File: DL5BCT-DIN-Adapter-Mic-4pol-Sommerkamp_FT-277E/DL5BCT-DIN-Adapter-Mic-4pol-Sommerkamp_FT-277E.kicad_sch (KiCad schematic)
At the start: 1 part

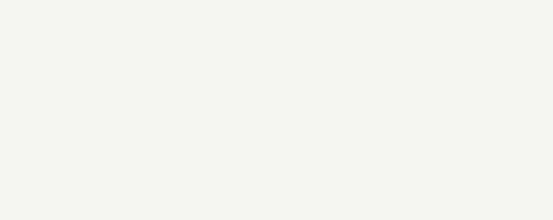
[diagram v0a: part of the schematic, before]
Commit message: Added new local schematics library for new symbols. 	modified:   DL5BCT-DIN-Adapter-Mic-4pol-Sommerkamp_FT-277E/DL5BCT-DIN-Adapter-Mic-4pol-Sommerkamp_FT-277E.kicad_sch 	new file:   DL5BCT-DIN-Adapter-Mic-4pol-Sommerkamp_FT-277E/sym-lib-table 	new file:   DL5BCT-DIN-Standard.bak 	new file:   DL5BCT-DIN-Standard.kicad_sym
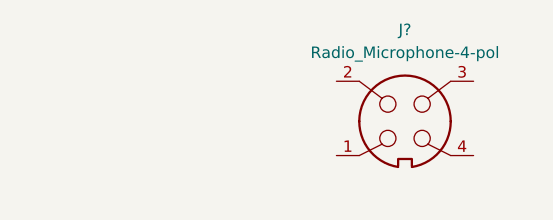
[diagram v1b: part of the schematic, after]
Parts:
- added J?: Radio_Microphone-4-pol, symbol DL5BCT-DIN-Standard:Radio_Microphone-4-pol
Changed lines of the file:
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@@
     (pin "5")
+  )
+  (symbol (lib_id "DL5BCT-DIN-Standard:Radio_Microphone-4-pol") (at 182.88 90.17 0) (unit 1)
+    (in_bom yes) (on_board yes) (fields_autoplaced)
+    (property "Reference" "J?" (id 0) (at 190.5 76.2 0))
+    (property "Value" "Radio_Microphone-4-pol" (id 1) (at 190.5 78.74 0))
+    (property "Footprint" "" (id 2) (at 190.5 86.36 0)
+      (effects (font (size 1.27 1.27)) hide)
+    )
+    (property "Datasheet" "(TBD)" (id 3) (at 190.5 95.25 0)
+      (effects (font (size 1.27 1.27)) hide)
+    )
+    (pin "1")
+    (pin "2")
+    (pin "3")
+    (pin "4")
   )
   (sheet_instances
@@
       (reference "J?") (unit 1) (value "DIN-5_180degree") (footprint "")
     )
+    (path "/8333ab48-756e-44fd-9bca-2278a8572e12"
+      (reference "J?") (unit 1) (value "Radio_Microphone-4-pol") (footprint "")
+    )
   )

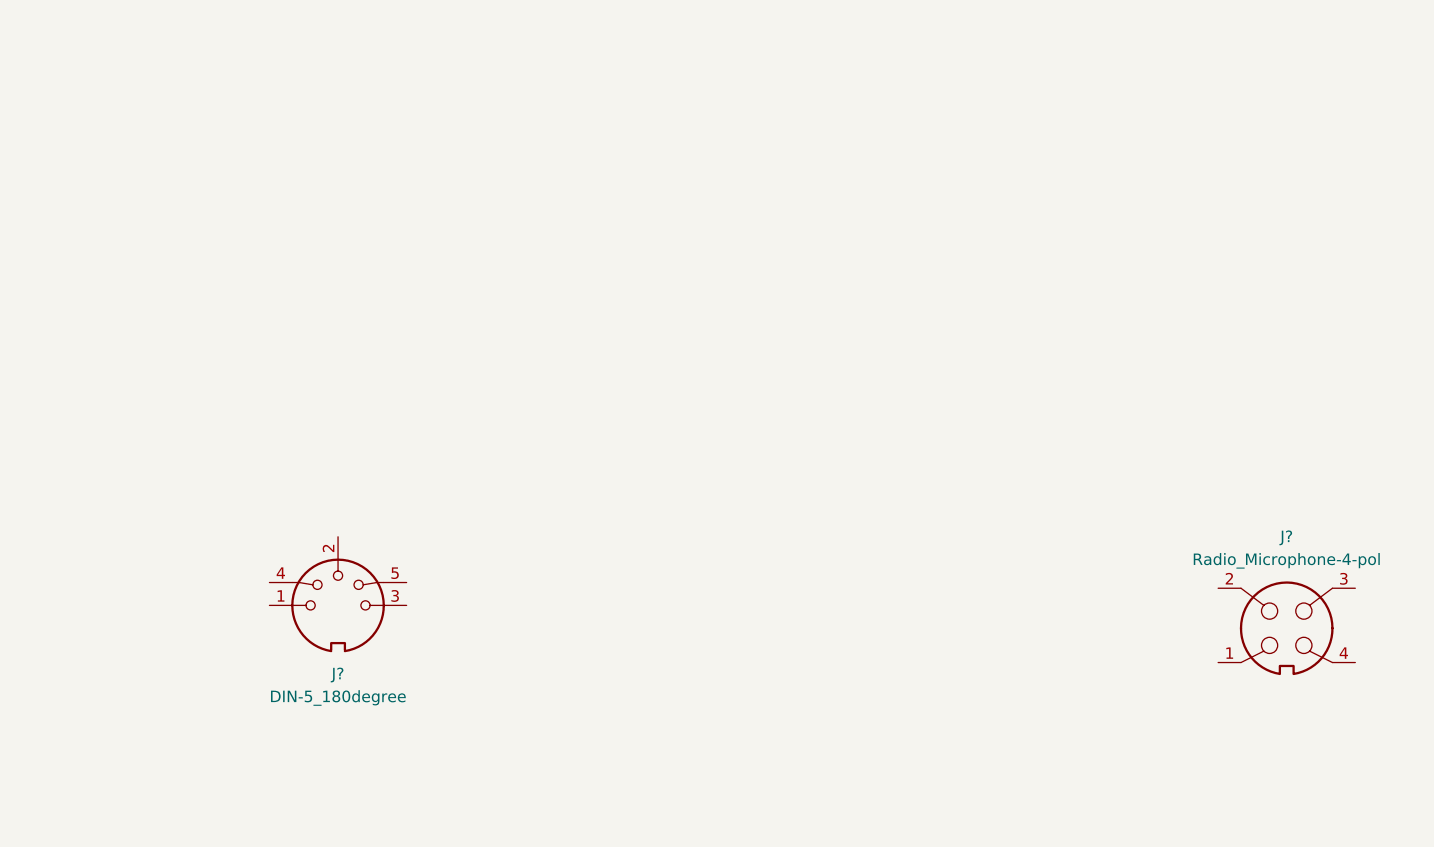
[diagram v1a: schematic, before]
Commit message: Complete adapter drawing. 	new file:   DL5BCT-DIN-Adapter-Mic-4pol-Sommerkamp_FT-277E/DL5BCT-DIN-Adapter-Mic-4pol-Sommerkamp_FT-277E.csv 	modified:   DL5BCT-DIN-Adapter-Mic-4pol-Sommerkamp_FT-277E/DL5BCT-DIN-Adapter-Mic-4pol-Sommerkamp_FT-277E.kicad_sch 	new file:   DL5BCT-DIN-Adapter-Mic-4pol-Sommerkamp_FT-277E/DL5BCT-DIN-Adapter-Mic-4pol-Sommerkamp_FT-277E.xml 	modified:   DL5BCT-DIN-Standard.bak 	modified:   DL5BCT-DIN-Standard.kicad_sym
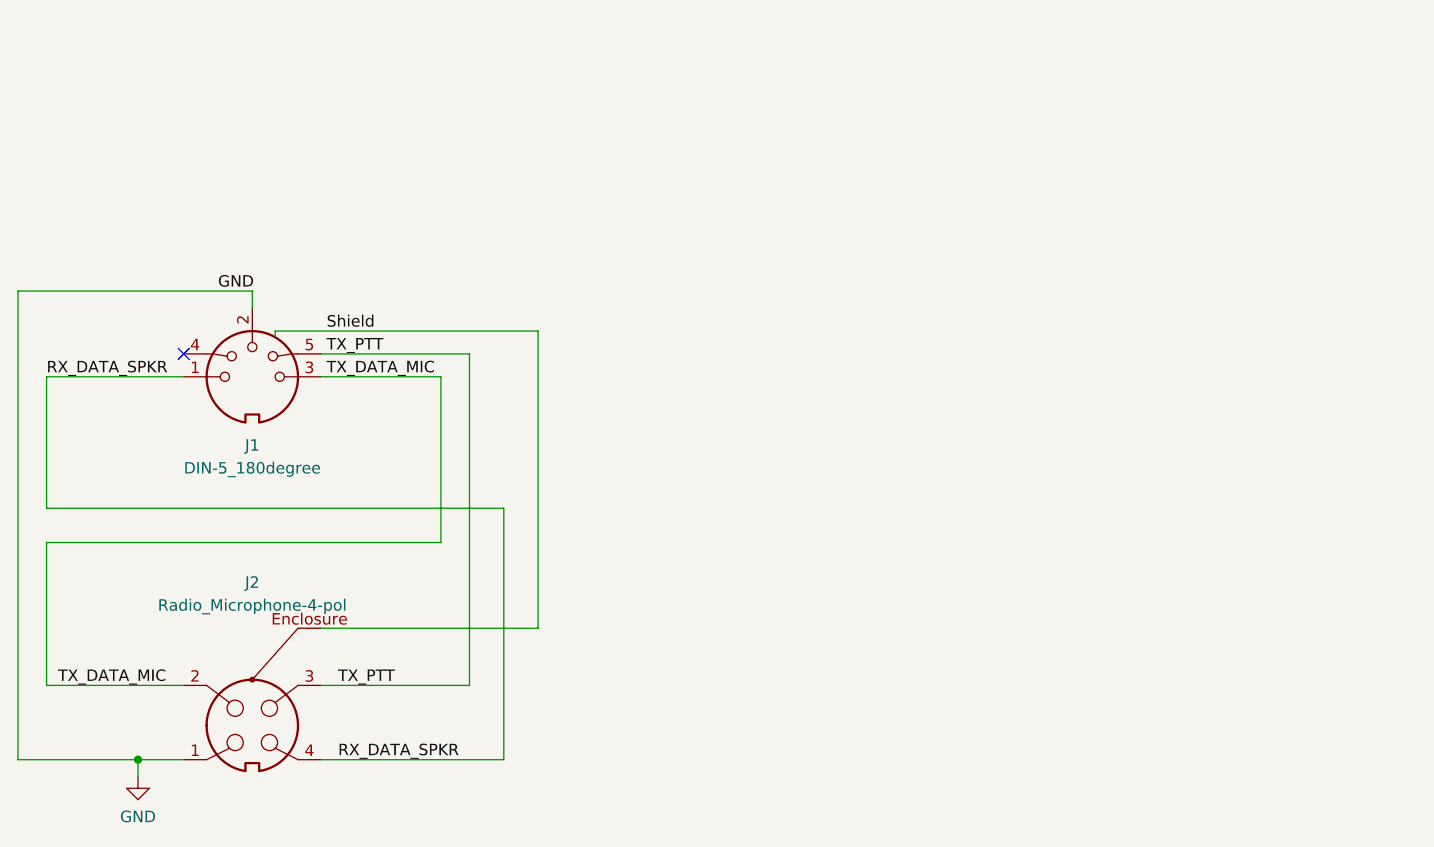
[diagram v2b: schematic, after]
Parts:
- removed J?: Radio_Microphone-4-pol, symbol DL5BCT-DIN-Standard:Radio_Microphone-4-pol
- added J2: Radio_Microphone-4-pol, symbol DL5BCT-DIN-Standard:Radio_Microphone-4-pol
- gave numbers to parts that had none: 1
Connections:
- net RX_DATA_SPKR: now reaches J1.1
- net RX_DATA_SPKR: now also J2.4
- net GND: now reaches J1.2
- net GND: now also J2.1
- net TX_DATA_MIC: now reaches J1.3
- net TX_DATA_MIC: now also J2.2
- net TX_PTT: now reaches J1.5
- net TX_PTT: now also J2.3
- new net Shield: J2.Enclosure
- no-connect marks 0 -> 1
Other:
- company: (none) -> Peter Cornelius DL5BCT / peter cornelius consulting
- title: (none) -> Adapter DL5BCT-DIN-Standard <--> TRX MIC 4-pol
- moved on the sheet: J1
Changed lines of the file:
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@@
 (kicad_sch (version 20211123) (generator eeschema)
-  (paper "A4")
-  (symbol (lib_id "Connector:DIN-5_180degree") (at 85.09 83.82 0) (unit 1)
+  (paper "A5" portrait)
+  (title_block
+    (title "Adapter DL5BCT-DIN-Standard <--> TRX MIC 4-pol")
+    (date "2023-01-07")
+    (rev "1.0")
+    (company "Peter Cornelius DL5BCT / peter cornelius consulting")
+    (comment 1 "Adapter from/to DL5BCT DIN Standard to 4-pol TRX mike connector")
+    (comment 2 "Sommerkamp FT-277 E")
+  )
+  (junction (at 62.865 100.965) (diameter 0) (color 0 0 0 0)
+  )
+  (no_connect (at 67.945 55.88))
+  (wire (pts (xy 52.705 73.025) (xy 52.705 58.42))
+    (stroke (width 0) (type default) (color 0 0 0 0))
+  )
+  (wire (pts (xy 96.52 76.835) (xy 96.52 58.42))
+    (stroke (width 0) (type default) (color 0 0 0 0))
+  )
+  (wire (pts (xy 62.865 100.965) (xy 67.945 100.965))
+    (stroke (width 0) (type default) (color 0 0 0 0))
+  )
+  (wire (pts (xy 78.105 53.34) (xy 78.105 53.975))
+    (stroke (width 0) (type default) (color 0 0 0 0))
+  )
+  (wire (pts (xy 52.705 92.71) (xy 52.705 76.835))
+    (stroke (width 0) (type default) (color 0 0 0 0))
+  )
+  (wire (pts (xy 52.705 76.835) (xy 96.52 76.835))
+    (stroke (width 0) (type default) (color 0 0 0 0))
+  )
+  (wire (pts (xy 75.565 48.895) (xy 75.565 50.8))
+    (stroke (width 0) (type default) (color 0 0 0 0))
+  )
+  (wire (pts (xy 83.185 86.36) (xy 107.315 86.36))
+    (stroke (width 0) (type default) (color 0 0 0 0))
+  )
+  (wire (pts (xy 103.505 73.025) (xy 52.705 73.025))
+    (stroke (width 0) (type default) (color 0 0 0 0))
+  )
+  (wire (pts (xy 107.315 86.36) (xy 107.315 53.34))
+    (stroke (width 0) (type default) (color 0 0 0 0))
+  )
+  (wire (pts (xy 99.695 55.88) (xy 83.185 55.88))
+    (stroke (width 0) (type default) (color 0 0 0 0))
+  )
+  (wire (pts (xy 49.53 100.965) (xy 62.865 100.965))
+    (stroke (width 0) (type default) (color 0 0 0 0))
+  )
+  (wire (pts (xy 83.185 92.71) (xy 99.695 92.71))
+    (stroke (width 0) (type default) (color 0 0 0 0))
+  )
+  (wire (pts (xy 83.185 100.965) (xy 103.505 100.965))
+    (stroke (width 0) (type default) (color 0 0 0 0))
+  )
+  (wire (pts (xy 52.705 92.71) (xy 67.945 92.71))
+    (stroke (width 0) (type default) (color 0 0 0 0))
+  )
+  (wire (pts (xy 49.53 48.895) (xy 49.53 100.965))
+    (stroke (width 0) (type default) (color 0 0 0 0))
+  )
+  (wire (pts (xy 49.53 48.895) (xy 75.565 48.895))
+    (stroke (width 0) (type default) (color 0 0 0 0))
+  )
+  (wire (pts (xy 107.315 53.34) (xy 78.105 53.34))
+    (stroke (width 0) (type default) (color 0 0 0 0))
+  )
+  (wire (pts (xy 96.52 58.42) (xy 83.185 58.42))
+    (stroke (width 0) (type default) (color 0 0 0 0))
+  )
+  (wire (pts (xy 62.865 100.965) (xy 62.865 102.87))
+    (stroke (width 0) (type default) (color 0 0 0 0))
+  )
+  (wire (pts (xy 52.705 58.42) (xy 67.945 58.42))
+    (stroke (width 0) (type default) (color 0 0 0 0))
+  )
+  (wire (pts (xy 103.505 100.965) (xy 103.505 73.025))
+    (stroke (width 0) (type default) (color 0 0 0 0))
+  )
+  (wire (pts (xy 99.695 92.71) (xy 99.695 55.88))
+    (stroke (width 0) (type default) (color 0 0 0 0))
+  )
+  (label "Shield" (at 83.82 53.34 0)
+    (effects (font (size 1.27 1.27)) (justify left bottom))
+  )
+  (label "TX_PTT" (at 85.09 92.71 0)
+    (effects (font (size 1.27 1.27)) (justify left bottom))
+  )
+  (label "TX_DATA_MIC" (at 53.975 92.71 0)
+    (effects (font (size 1.27 1.27)) (justify left bottom))
+  )
+  (label "TX_PTT" (at 83.82 55.88 0)
+    (effects (font (size 1.27 1.27)) (justify left bottom))
+  )
+  (label "TX_DATA_MIC" (at 83.82 58.42 0)
+    (effects (font (size 1.27 1.27)) (justify left bottom))
+  )
+  (label "RX_DATA_SPKR" (at 52.705 58.42 0)
+    (effects (font (size 1.27 1.27)) (justify left bottom))
+  )
+  (label "RX_DATA_SPKR" (at 85.09 100.965 0)
+    (effects (font (size 1.27 1.27)) (justify left bottom))
+  )
+  (label "GND" (at 71.755 48.895 0)
+    (effects (font (size 1.27 1.27)) (justify left bottom))
+  )
+  (symbol (lib_id "Connector:DIN-5_180degree") (at 75.565 58.42 0) (unit 1)
     (in_bom yes) (on_board yes) (fields_autoplaced)
-    (property "Reference" "J?" (id 0) (at 85.0901 91.44 0))
-    (property "Value" "DIN-5_180degree" (id 1) (at 85.0901 93.98 0))
-    (property "Footprint" "" (id 2) (at 85.09 83.82 0)
+    (property "Reference" "J1" (id 0) (at 75.5651 66.04 0))
+    (property "Value" "DIN-5_180degree" (id 1) (at 75.5651 68.58 0))
+    (property "Footprint" "" (id 2) (at 75.565 58.42 0)
       (effects (font (size 1.27 1.27)) hide)
     )
-    (property "Datasheet" "http://www.mouser.com/ds/2/18/40_c091_abd_e-75918.pdf" (id 3) (at 85.09 83.82 0)
+    (property "Datasheet" "http://www.mouser.com/ds/2/18/40_c091_abd_e-75918.pdf" (id 3) (at 75.565 58.42 0)
       (effects (font (size 1.27 1.27)) hide)
     )
@@
     (pin "5")
   )
-  (symbol (lib_id "DL5BCT-DIN-Standard:Radio_Microphone-4-pol") (at 182.88 90.17 0) (unit 1)
+  (symbol (lib_id "DL5BCT-DIN-Standard:Radio_Microphone-4-pol") (at 67.945 100.965 0) (unit 1)
     (in_bom yes) (on_board yes) (fields_autoplaced)
-    (property "Reference" "J?" (id 0) (at 190.5 76.2 0))
-    (property "Value" "Radio_Microphone-4-pol" (id 1) (at 190.5 78.74 0))
-    (property "Footprint" "" (id 2) (at 190.5 86.36 0)
+    (property "Reference" "J2" (id 0) (at 75.565 81.28 0))
+    (property "Value" "Radio_Microphone-4-pol" (id 1) (at 75.565 83.82 0))
+    (property "Footprint" "" (id 2) (at 75.565 97.155 0)
       (effects (font (size 1.27 1.27)) hide)
     )
-    (property "Datasheet" "(TBD)" (id 3) (at 190.5 95.25 0)
+    (property "Datasheet" "(TBD)" (id 3) (at 75.565 108.585 0)
       (effects (font (size 1.27 1.27)) hide)
     )
@@
     (pin "3")
     (pin "4")
+    (pin "Enclosure")
+  )
+  (symbol (lib_id "power:GND") (at 62.865 102.87 0) (unit 1)
+    (in_bom yes) (on_board yes) (fields_autoplaced)
+    (property "Reference" "#PWR01" (id 0) (at 62.865 109.22 0)
+      (effects (font (size 1.27 1.27)) hide)
+    )
+    (property "Value" "GND" (id 1) (at 62.865 107.315 0))
+    (property "Footprint" "" (id 2) (at 62.865 102.87 0)
+      (effects (font (size 1.27 1.27)) hide)
+    )
+    (property "Datasheet" "" (id 3) (at 62.865 102.87 0)
+      (effects (font (size 1.27 1.27)) hide)
+    )
+    (pin "1")
   )
   (sheet_instances
@@
   )
   (symbol_instances
+    (path "/a2761d60-33b1-4204-8aee-7e96a47641a1"
+      (reference "#PWR01") (unit 1) (value "GND") (footprint "")
+    )
     (path "/2272e953-9a54-47b8-a2b5-620e9d30e3a1"
-      (reference "J?") (unit 1) (value "DIN-5_180degree") (footprint "")
+      (reference "J1") (unit 1) (value "DIN-5_180degree") (footprint "")
     )
-    (path "/8333ab48-756e-44fd-9bca-2278a8572e12"
-      (reference "J?") (unit 1) (value "Radio_Microphone-4-pol") (footprint "")
+    (path "/774aba88-46ed-476c-91d0-61f7507cc184"
+      (reference "J2") (unit 1) (value "Radio_Microphone-4-pol") (footprint "")
     )
   )

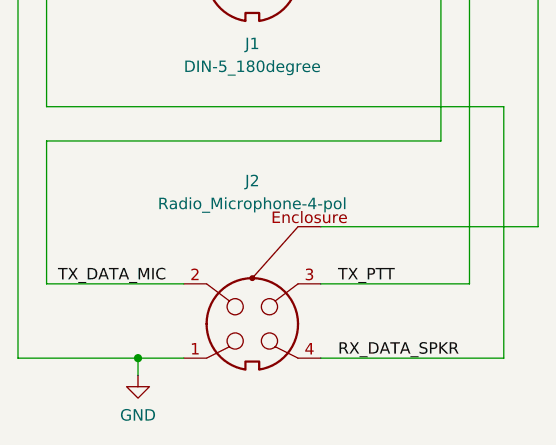
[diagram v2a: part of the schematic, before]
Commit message: Updated drawing with updated 4-pin connector symbol. 	modified:   DL5BCT-DIN-Adapter-Mic-4pol-Sommerkamp_FT-277E/DL5BCT-DIN-Adapter-Mic-4pol-Sommerkamp_FT-277E.kicad_sch
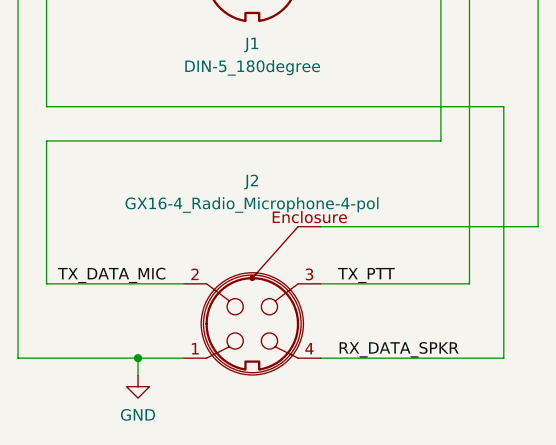
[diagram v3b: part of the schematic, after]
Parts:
- removed J2: Radio_Microphone-4-pol, symbol DL5BCT-DIN-Standard:Radio_Microphone-4-pol
- added J2: GX16-4_Radio_Microphone-4-pol, symbol DL5BCT-DIN-Standard:GX16-4_Radio_Microphone-4-pol
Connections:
- net GND: now also J2.1
- net RX_DATA_SPKR: now also J2.4
- net Shield: now also J2.Enclosure
- net TX_DATA_MIC: now also J2.2
- net TX_PTT: now also J2.3
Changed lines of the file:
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@@
     (pin "5")
-  )
-  (symbol (lib_id "DL5BCT-DIN-Standard:Radio_Microphone-4-pol") (at 67.945 100.965 0) (unit 1)
-    (in_bom yes) (on_board yes) (fields_autoplaced)
-    (property "Reference" "J2" (id 0) (at 75.565 81.28 0))
-    (property "Value" "Radio_Microphone-4-pol" (id 1) (at 75.565 83.82 0))
-    (property "Footprint" "" (id 2) (at 75.565 97.155 0)
-      (effects (font (size 1.27 1.27)) hide)
-    )
-    (property "Datasheet" "(TBD)" (id 3) (at 75.565 108.585 0)
-      (effects (font (size 1.27 1.27)) hide)
-    )
-    (pin "1")
-    (pin "2")
-    (pin "3")
-    (pin "4")
-    (pin "Enclosure")
   )
   (symbol (lib_id "power:GND") (at 62.865 102.87 0) (unit 1)
@@
     (pin "1")
   )
+  (symbol (lib_id "DL5BCT-DIN-Standard:GX16-4_Radio_Microphone-4-pol") (at 67.945 100.965 0) (unit 1)
+    (in_bom yes) (on_board yes) (fields_autoplaced)
+    (property "Reference" "J2" (id 0) (at 75.565 81.28 0))
+    (property "Value" "GX16-4_Radio_Microphone-4-pol" (id 1) (at 75.565 83.82 0))
+    (property "Footprint" "" (id 2) (at 75.565 97.155 0)
+      (effects (font (size 1.27 1.27)) hide)
+    )
+    (property "Datasheet" "https://cdn-reichelt.de/documents/datenblatt/C160/M604.pdf" (id 3) (at 75.565 109.855 0)
+      (effects (font (size 1.27 1.27)) hide)
+    )
+    (property "Datasheet2" "https://www.renhotecpro.com/wp-content/uploads/2017/04/GX-Series-Aviation-Connectors-Presentation.pdf" (id 4) (at 67.945 112.395 0)
+      (effects (font (size 1.27 1.27)) hide)
+    )
+    (pin "1")
+    (pin "2")
+    (pin "3")
+    (pin "4")
+    (pin "Enclosure")
+  )
   (sheet_instances
     (path "/" (page "1"))
@@
       (reference "J1") (unit 1) (value "DIN-5_180degree") (footprint "")
     )
-    (path "/774aba88-46ed-476c-91d0-61f7507cc184"
-      (reference "J2") (unit 1) (value "Radio_Microphone-4-pol") (footprint "")
+    (path "/c96b8aac-8d3f-4e01-ac79-d040f523e53e"
+      (reference "J2") (unit 1) (value "GX16-4_Radio_Microphone-4-pol") (footprint "")
     )
   )

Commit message: Corrected language typo in sheet title block. 	modified:   DL5BCT-DIN-Adapter-Mic-4pol-Sommerkamp_FT-277E/DL5BCT-DIN-Adapter-Mic-4pol-Sommerkamp_FT-277E.kicad_sch
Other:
- title: Adapter DL5BCT-DIN-Standard <--> TRX MIC 4-pol -> Adaptor DL5BCT-DIN-Standard <--> TRX MIC 4-pol
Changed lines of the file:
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@@
   (paper "A5" portrait)
   (title_block
-    (title "Adapter DL5BCT-DIN-Standard <--> TRX MIC 4-pol")
+    (title "Adaptor DL5BCT-DIN-Standard <--> TRX MIC 4-pol")
     (date "2023-01-07")
     (rev "1.0")
     (company "Peter Cornelius DL5BCT / peter cornelius consulting")
-    (comment 1 "Adapter from/to DL5BCT DIN Standard to 4-pol TRX mike connector")
+    (comment 1 "Adaptor from/to DL5BCT DIN Standard to 4-pol TRX mike connector")
     (comment 2 "Sommerkamp FT-277 E")
   )
